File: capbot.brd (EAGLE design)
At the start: 43.2 x 49 mm, 55 parts, among them J1 USBPCB, J2 USBPCB, J3 USBPCB

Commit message: r1
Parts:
- added U$11, U$13, U$15, U$17, U$19, U$21: (no value), cwlogo:ON
- added U$12, U$14, U$16, U$18, U$20, U$7: (no value), cwlogo:OFF
- LED1, LED2, LED3, LED4, LED5, LED6: device led:LED3MM -> cwpackage:LED3MM-MOREFLAT
- moved PAD1 0.10 mm to (36.7, 11.6)
- moved PAD11 0.10 mm to (36.7, 15.4)
- moved PAD3 0.10 mm to (36.7, 1.42)
- moved PAD9 0.10 mm to (36.7, 25.6)
- moved PAD10 0.10 mm to (39.3, 25.6)
- moved PAD12 0.10 mm to (39.3, 15.4)
- moved PAD2 0.10 mm to (39.3, 11.6)
- moved PAD4 0.10 mm to (39.3, 1.42)
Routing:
- added copper zone on layer 16, net N$1
- added copper zone on layer 16, net N$11
- added copper zone on layer 16, net N$12
- added copper zone on layer 16, net N$2
- added copper zone on layer 16, net N$21
- added copper zone on layer 16, net N$22
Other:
- outline, holes or cut-outs redrawn

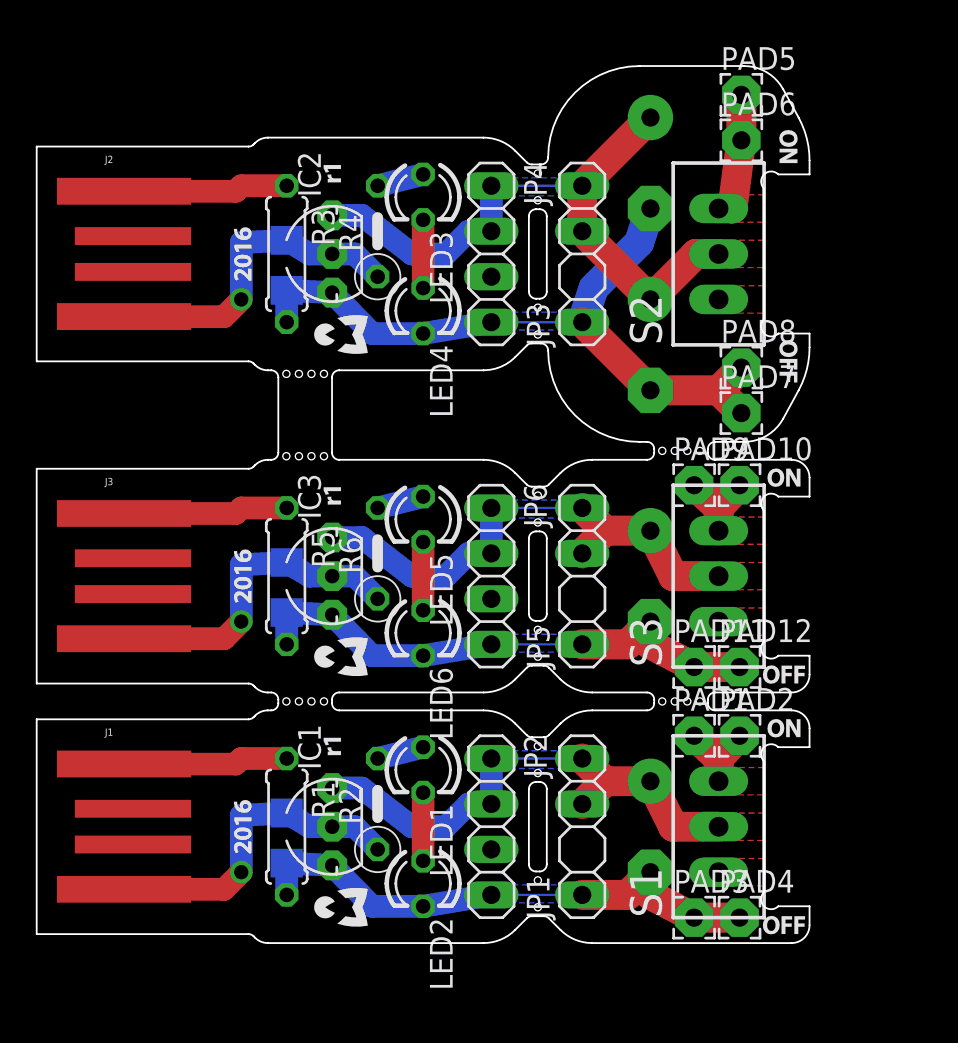
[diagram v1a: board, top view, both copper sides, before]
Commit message: Stretch the charger part by 0.2 in.
This goes against my natural tendency to make things as small as possible, but in this case the added length has some advantages:
- It allows the use of a straight instead of angled pin header if desired, without the switch getting in the way of the USB port.
- It makes things a bit easier to solder for beginners.
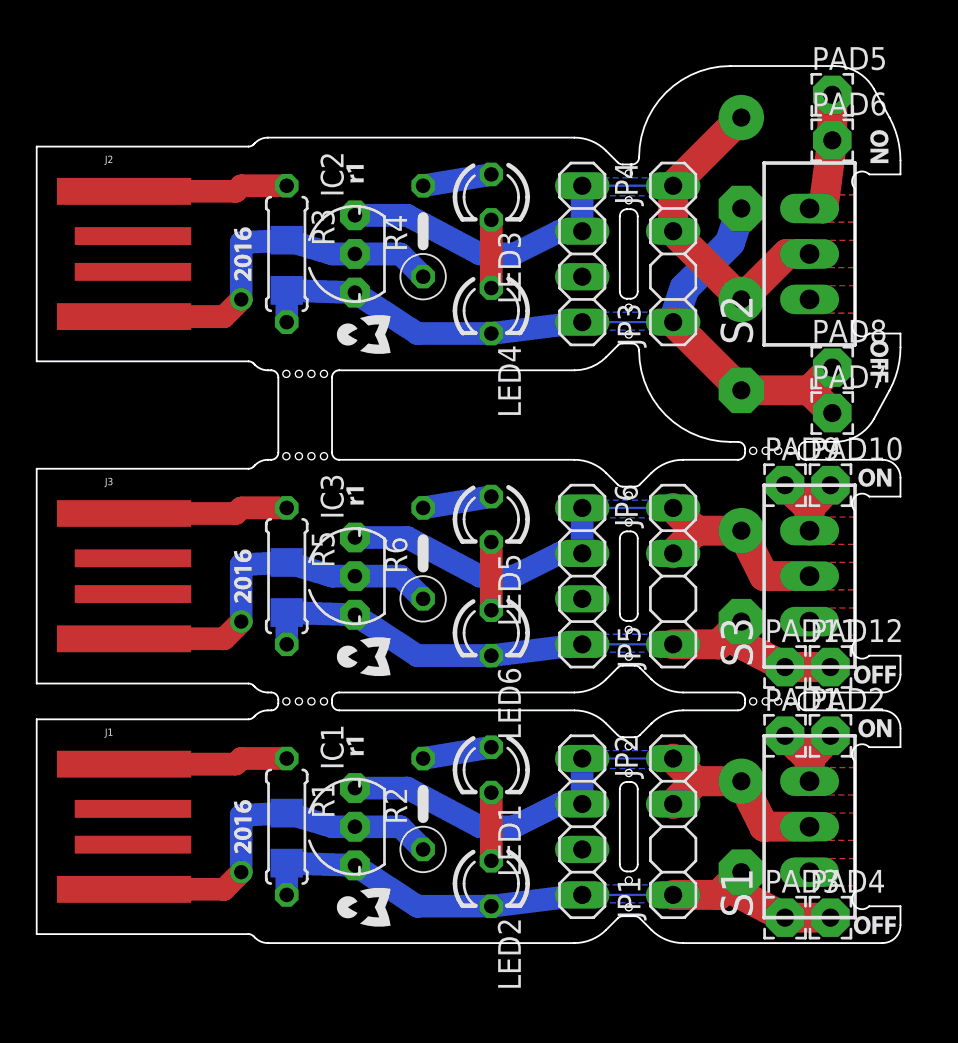
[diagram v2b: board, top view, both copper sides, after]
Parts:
- moved PAD1 5.08 mm to (41.8, 11.6)
- moved PAD11 5.08 mm to (41.8, 15.4)
- moved PAD3 5.08 mm to (41.8, 1.42)
- moved PAD5 5.08 mm to (44.5, 47.4)
- moved PAD6 5.08 mm to (44.5, 44.9)
- moved PAD7 5.08 mm to (44.5, 29.6)
- moved PAD8 5.08 mm to (44.5, 32.1)
- moved PAD9 5.08 mm to (41.8, 25.6)
- moved JP1 5.08 mm to (35.6, 6.50)
- moved JP2 5.08 mm to (30.5, 6.50)
- moved JP3 5.08 mm to (35.6, 38.5)
- moved JP4 5.08 mm to (30.5, 38.5)
- moved JP5 5.08 mm to (35.6, 20.5)
- moved JP6 5.08 mm to (30.5, 20.5)
- moved C1 5.08 mm to (39.4, 6.50)
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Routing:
- net N$11: track 39.7 -> 44.5 mm
- net N$1: track 30.2 -> 35.0 mm
- net N$21: track 30.2 -> 35.0 mm
- net N$2: track 29.3 -> 32.7 mm
- net N$12: track 36.0 -> 39.3 mm
- net N$22: track 29.3 -> 32.7 mm
- net N$26: track 18.5 -> 20.9 mm
- net N$6: track 18.5 -> 20.9 mm
- net N$16: track 18.5 -> 20.9 mm
- net N$18: track 2.62 -> 3.86 mm
- net N$8: track 2.62 -> 3.86 mm
- net N$28: track 2.62 -> 3.86 mm
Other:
- board size 43.2 x 49 mm -> 48.3 x 49 mm

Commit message: Move the pin header 0.8 mm closer to the edge so that the horizontal part of the wires can sit flush to the surface with less bending and filing.
This required changing the pads from "long" to "offset" to prevent them from getting too close to the edge. Unfortunately it seems a pad can only be offset all the way, the drill position is not continuously adjustable - I'd have preferred something in between.
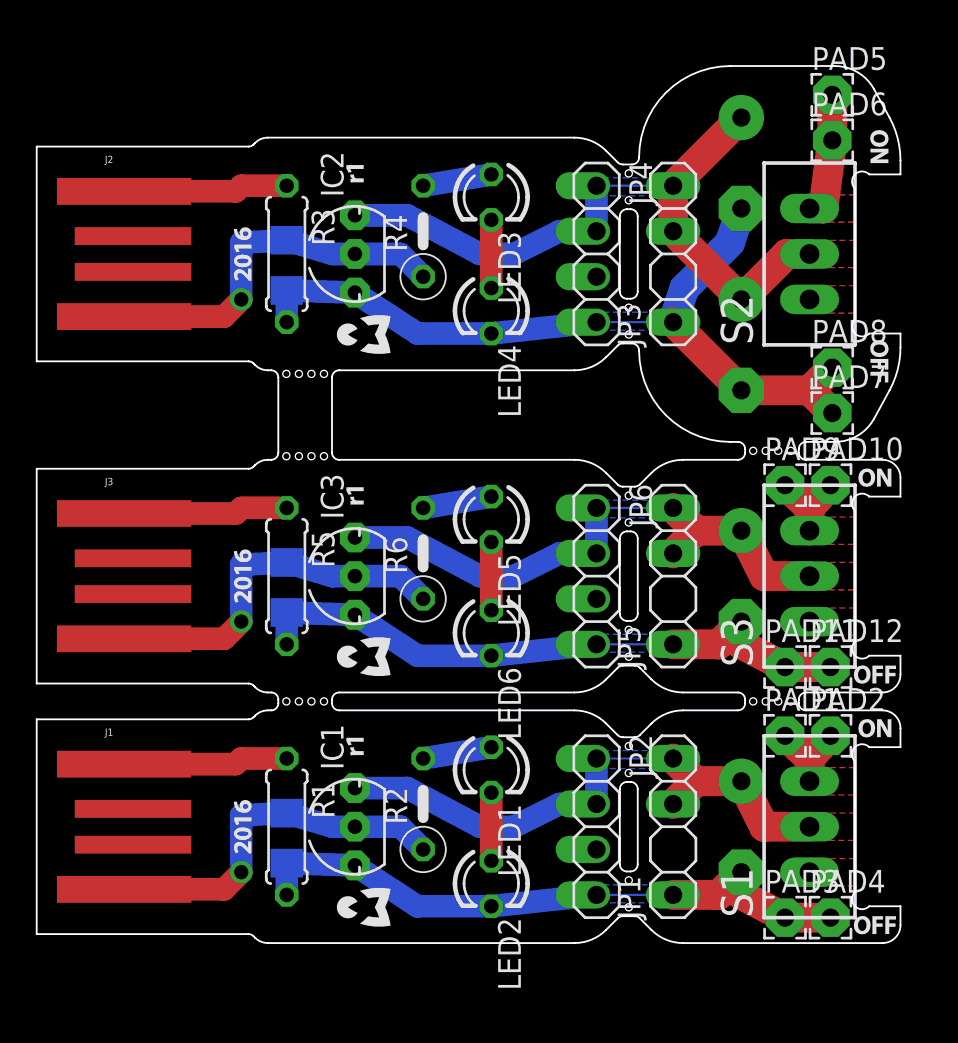
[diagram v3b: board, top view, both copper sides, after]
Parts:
- JP2, JP4, JP6: device pinhead:1X04 -> cwpinhead:1X04/OFFSETDOWN
- moved JP2 0.80 mm to (31.3, 6.50)
- moved JP4 0.80 mm to (31.3, 38.5)
- moved JP6 0.80 mm to (31.3, 20.5)
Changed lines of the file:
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@@
 <element name="LED1" library="cwpackage" package="LED3MM-MOREFLAT" value="" x="25.4" y="9.675" rot="R270"/>
 <element name="LED2" library="cwpackage" package="LED3MM-MOREFLAT" value="" x="25.4" y="3.325" rot="R270"/>
-<element name="JP2" library="pinhead" package="1X04" value="" x="30.48" y="6.5" rot="R270"/>
+<element name="JP2" library="cwpinhead" package="1X04/OFFSETDOWN" value="" x="31.28" y="6.5" rot="R270"/>
 <element name="J1" library="SparkFun-Connectors" package="USB-A-PCB" value="USBPCB" x="5.08" y="6.5"/>
 <element name="C3" library="resistor" package="E5-10,5" value="" x="39.37" y="33.42" rot="MR270"/>
@@
 <element name="LED3" library="cwpackage" package="LED3MM-MOREFLAT" value="" x="25.4" y="41.675" rot="R270"/>
 <element name="LED4" library="cwpackage" package="LED3MM-MOREFLAT" value="" x="25.4" y="35.325" rot="R270"/>
-<element name="JP4" library="pinhead" package="1X04" value="" x="30.48" y="38.5" rot="R270"/>
+<element name="JP4" library="cwpinhead" package="1X04/OFFSETDOWN" value="" x="31.28" y="38.5" rot="R270"/>
 <element name="J2" library="SparkFun-Connectors" package="USB-A-PCB" value="USBPCB" x="5.08" y="38.5"/>
 <element name="C5" library="resistor" package="E5-10,5" value="" x="39.37" y="43.58" rot="MR270"/>
@@
 <element name="LED5" library="cwpackage" package="LED3MM-MOREFLAT" value="" x="25.4" y="23.675" rot="R270"/>
 <element name="LED6" library="cwpackage" package="LED3MM-MOREFLAT" value="" x="25.4" y="17.325" rot="R270"/>
-<element name="JP6" library="pinhead" package="1X04" value="" x="30.48" y="20.5" rot="R270"/>
+<element name="JP6" library="cwpinhead" package="1X04/OFFSETDOWN" value="" x="31.28" y="20.5" rot="R270"/>
 <element name="J3" library="SparkFun-Connectors" package="USB-A-PCB" value="USBPCB" x="5.08" y="20.5"/>
 <element name="U$8" library="cwlogo" package="CWLOGO-3" value="" x="18.27" y="16" rot="R90"/>
@@
 <wire x1="17.78" y1="4.341" x2="21.2725" y2="2.055" width="1.27" layer="16"/>
 <wire x1="21.2725" y1="2.055" x2="25.4" y2="2.055" width="1.27" layer="16"/>
-<wire x1="25.4" y1="2.055" x2="30.48" y2="2.69" width="1.27" layer="16"/>
-<wire x1="30.48" y1="2.69" x2="35.56" y2="2.69" width="0.127" layer="16"/>
+<wire x1="25.4" y1="2.055" x2="31.28" y2="2.69" width="1.27" layer="16"/>
+<wire x1="31.28" y1="2.69" x2="35.56" y2="2.69" width="0.127" layer="16"/>
 <polygon width="0.127" layer="16" thermals="no">
 <vertex x="30.58" y="3.25"/>
@@
 <wire x1="24.765" y1="6.5" x2="26.67" y2="6.5" width="1.27" layer="16"/>
 <wire x1="26.67" y1="6.5" x2="29.21" y2="7.77" width="1.27" layer="16"/>
-<wire x1="29.21" y1="7.77" x2="30.48" y2="7.77" width="1.27" layer="16"/>
-<wire x1="30.48" y1="7.77" x2="30.48" y2="10.31" width="1.27" layer="16"/>
-<wire x1="30.48" y1="10.31" x2="35.56" y2="10.31" width="0.127" layer="16"/>
+<wire x1="29.21" y1="7.77" x2="31.28" y2="7.77" width="1.27" layer="16"/>
+<wire x1="31.28" y1="7.77" x2="31.28" y2="10.31" width="1.27" layer="16"/>
+<wire x1="31.28" y1="10.31" x2="35.56" y2="10.31" width="0.127" layer="16"/>
 <polygon width="0.127" layer="16" thermals="no">
 <vertex x="30.58" y="10.75"/>
@@
 <wire x1="17.78" y1="36.341" x2="21.2725" y2="34.055" width="1.27" layer="16"/>
 <wire x1="21.2725" y1="34.055" x2="25.4" y2="34.055" width="1.27" layer="16"/>
-<wire x1="25.4" y1="34.055" x2="30.48" y2="34.69" width="1.27" layer="16"/>
-<wire x1="30.48" y1="34.69" x2="35.56" y2="34.69" width="0.127" layer="16"/>
+<wire x1="25.4" y1="34.055" x2="31.28" y2="34.69" width="1.27" layer="16"/>
+<wire x1="31.28" y1="34.69" x2="35.56" y2="34.69" width="0.127" layer="16"/>
 <contactref element="C5" pad="-"/>
 <wire x1="35.56" y1="34.69" x2="39.37" y2="30.88" width="1.6764" layer="1"/>
@@
 <wire x1="24.765" y1="38.5" x2="26.67" y2="38.5" width="1.27" layer="16"/>
 <wire x1="26.67" y1="38.5" x2="29.21" y2="39.77" width="1.27" layer="16"/>
-<wire x1="29.21" y1="39.77" x2="30.48" y2="39.77" width="1.27" layer="16"/>
-<wire x1="30.48" y1="39.77" x2="30.48" y2="42.31" width="1.27" layer="16"/>
-<wire x1="30.48" y1="42.31" x2="35.56" y2="42.31" width="0.127" layer="16"/>
+<wire x1="29.21" y1="39.77" x2="31.28" y2="39.77" width="1.27" layer="16"/>
+<wire x1="31.28" y1="39.77" x2="31.28" y2="42.31" width="1.27" layer="16"/>
+<wire x1="31.28" y1="42.31" x2="35.56" y2="42.31" width="0.127" layer="16"/>
 <contactref element="C5" pad="+"/>
 <wire x1="39.37" y1="46.12" x2="35.56" y2="42.31" width="1.6764" layer="1"/>
@@
 <wire x1="17.78" y1="18.341" x2="21.2725" y2="16.055" width="1.27" layer="16"/>
 <wire x1="21.2725" y1="16.055" x2="25.4" y2="16.055" width="1.27" layer="16"/>
-<wire x1="25.4" y1="16.055" x2="30.48" y2="16.69" width="1.27" layer="16"/>
-<wire x1="30.48" y1="16.69" x2="35.56" y2="16.69" width="0.127" layer="16"/>
+<wire x1="25.4" y1="16.055" x2="31.28" y2="16.69" width="1.27" layer="16"/>
+<wire x1="31.28" y1="16.69" x2="35.56" y2="16.69" width="0.127" layer="16"/>
 <polygon width="0.127" layer="16" thermals="no">
 <vertex x="30.58" y="17.25"/>
@@
 <wire x1="24.765" y1="20.5" x2="26.67" y2="20.5" width="1.27" layer="16"/>
 <wire x1="26.67" y1="20.5" x2="29.21" y2="21.77" width="1.27" layer="16"/>
-<wire x1="29.21" y1="21.77" x2="30.48" y2="21.77" width="1.27" layer="16"/>
-<wire x1="30.48" y1="21.77" x2="30.48" y2="24.31" width="1.27" layer="16"/>
-<wire x1="30.48" y1="24.31" x2="35.56" y2="24.31" width="0.127" layer="16"/>
+<wire x1="29.21" y1="21.77" x2="31.28" y2="21.77" width="1.27" layer="16"/>
+<wire x1="31.28" y1="21.77" x2="31.28" y2="24.31" width="1.27" layer="16"/>
+<wire x1="31.28" y1="24.31" x2="35.56" y2="24.31" width="0.127" layer="16"/>
 <polygon width="0.127" layer="16" thermals="no">
 <vertex x="30.58" y="24.75"/>
